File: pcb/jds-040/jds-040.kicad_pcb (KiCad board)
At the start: 2 copper layers, 18.1 x 21.5 mm, 9 parts, among them J1 USB_C_Receptacle_USB2.0, J2 FPC_01x12

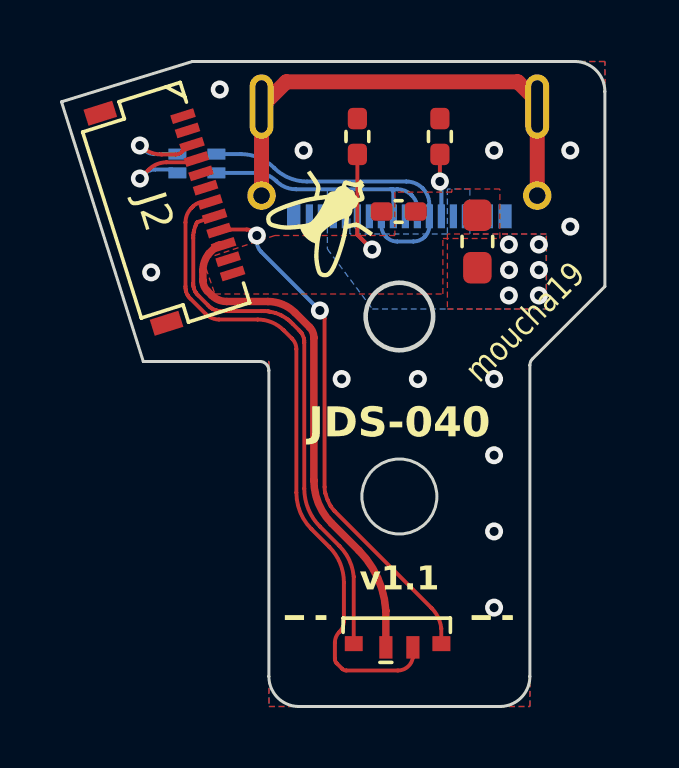
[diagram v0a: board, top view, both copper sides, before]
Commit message: Connected shield to ground just like in the original part.
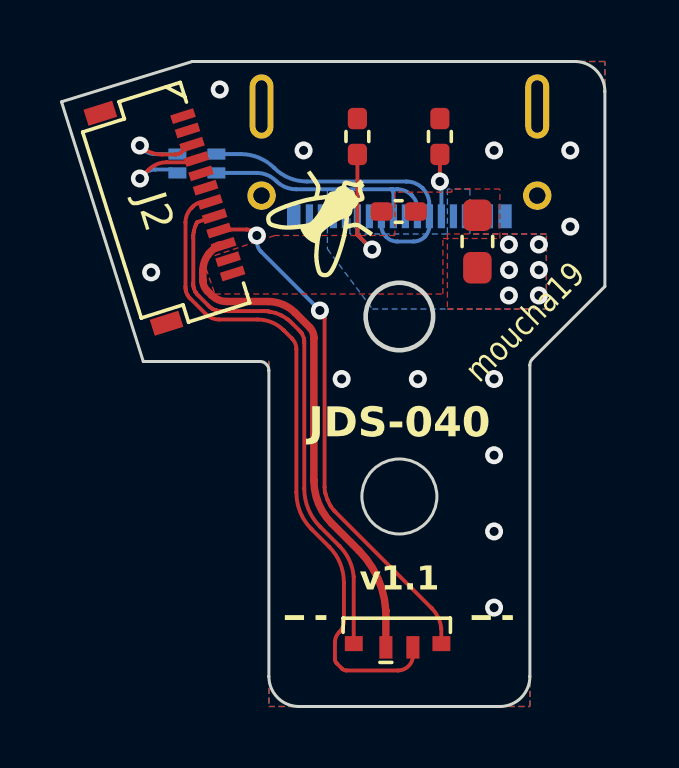
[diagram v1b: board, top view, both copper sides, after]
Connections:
- J1 pad S1: /SHIELD -> GND
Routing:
- net /SHIELD: track 16.1 -> 0.00 mm
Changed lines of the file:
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@@
     (rev "1.1")
     (company "Petr Moucha")
-    (comment 2 "Licensed under CERN-OHL-W v2")
+    (comment 2 "Any use or reproduction unrelated to this project is prohibited.")
+    (comment 3 "The fly logo is the property of Petr Moucha. ")
+    (comment 4 "Licensed under CERN-OHL-W v2")
   )
   (layers
@@
   (net 14 "Net-(J1-CC2)")
   (net 15 "unconnected-(J1-SBU2-PadB8)")
-  (net 16 "/SHIELD")
   (footprint "Capacitor_SMD:C_0402_1005Metric_Pad0.74x0.62mm_HandSolder" (layer "F.Cu")
     (at 96.041 64.278 180)
@@
       (net 2 "GND") (pinfunction "GND") (pintype "passive"))
     (pad "S1" thru_hole oval locked (at -4.595 0) (size 0.8 2.15) (drill oval 0.4 1.75) (layers "*.Cu" "*.Mask")
-      (net 16 "/SHIELD") (pinfunction "SHIELD") (pintype "passive"))
+      (net 2 "GND") (pinfunction "SHIELD") (pintype "passive"))
     (pad "S1" thru_hole circle locked (at -4.595 2.97) (size 0.95 0.95) (drill 0.55) (layers "*.Cu" "*.Mask")
-      (net 16 "/SHIELD") (pinfunction "SHIELD") (pintype "passive"))
+      (net 2 "GND") (pinfunction "SHIELD") (pintype "passive"))
     (pad "S1" thru_hole oval locked (at 4.595 0) (size 0.8 2.15) (drill oval 0.4 1.75) (layers "*.Cu" "*.Mask")
-      (net 16 "/SHIELD") (pinfunction "SHIELD") (pintype "passive"))
+      (net 2 "GND") (pinfunction "SHIELD") (pintype "passive"))
     (pad "S1" thru_hole circle locked (at 4.595 2.97) (size 0.95 0.95) (drill 0.55) (layers "*.Cu" "*.Mask")
-      (net 16 "/SHIELD") (pinfunction "SHIELD") (pintype "passive"))
+      (net 2 "GND") (pinfunction "SHIELD") (pintype "passive"))
     (model "${MOUCHA_LIB}/Moucha.3dshapes/USBC_Receptacle_TYPE-C-31-M-12.step"
       (offset (xyz -4.5 -3.5 0))
@@
   (segment (start 97.416 63.278) (end 97.441 63.303) (width 0.13) (layer "B.Cu") (net 14))
   (arc (start 97.466 63.363355) (mid 97.459502 63.330691) (end 97.441 63.303) (width 0.13) (layer "B.Cu") (net 14))
-  (segment (start 100.661 60.6005) (end 100.0165 59.956) (width 0.5) (layer "F.Cu") (net 16))
-  (segment (start 91.471 60.6005) (end 91.471 63.748) (width 0.5) (layer "F.Cu") (net 16))
-  (segment (start 92.293 59.956) (end 91.471 60.778) (width 0.5) (layer "F.Cu") (net 16))
-  (segment (start 100.661 63.748) (end 100.661 60.6005) (width 0.5) (layer "F.Cu") (net 16))
-  (segment (start 100.0165 59.956) (end 92.293 59.956) (width 0.5) (layer "F.Cu") (net 16))
   (zone (net 1) (net_name "VBUS") (layer "F.Cu") (hatch edge 0.5)
     (priority 2)

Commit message: Replaced fuse with a part that satisfies DS4 current rating, upgraded project to Kicad 8
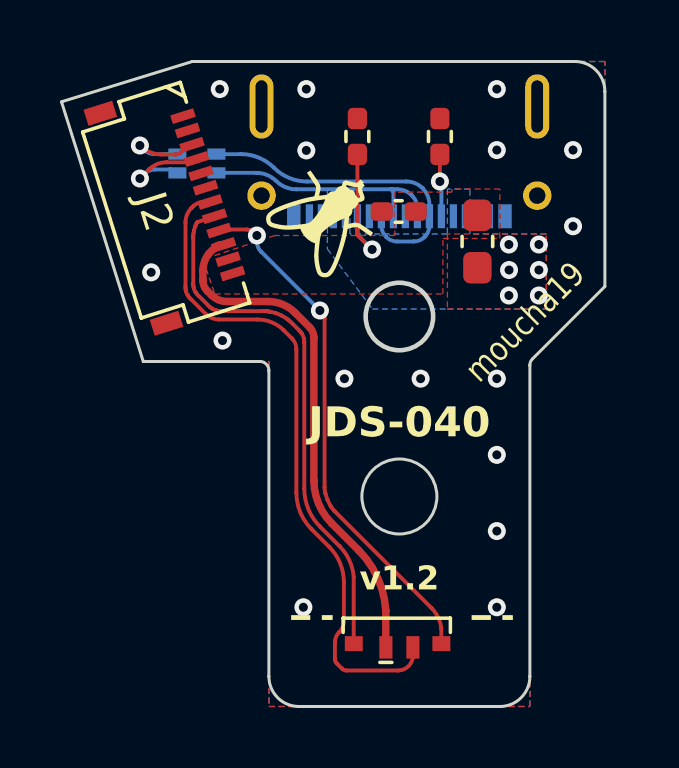
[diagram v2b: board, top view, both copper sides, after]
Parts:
- F2: value locked -> 750 mA
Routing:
- net GND: vias 12 -> 16

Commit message: Changed F2,D2 to F1,D1
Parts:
- renumbered D2 to D1, F2 to F1
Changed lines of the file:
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@@
 		(layer "F.Cu")
 		(at 96.066 78.808 180)
-		(property "Reference" "D2"
+		(property "Reference" "D1"
 			(at 0.05 2 0)
 			(unlocked yes)
@@
 		(descr "Fuse SMD 0603 (1608 Metric), square (rectangular) end terminal, IPC_7351 nominal with elongated pad for handsoldering. (Body size source: http://www.tortai-tech.com/upload/download/2011102023233369053.pdf), generated with kicad-footprint-generator")
 		(tags "fuse handsolder")
-		(property "Reference" "F2"
+		(property "Reference" "F1"
 			(at 0 1.414214 90)
 			(layer "F.SilkS")
